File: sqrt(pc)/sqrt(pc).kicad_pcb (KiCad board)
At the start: 2 copper layers, 64 x 39.5 mm, 14 parts, among them U1 WEMOS_C3_mini

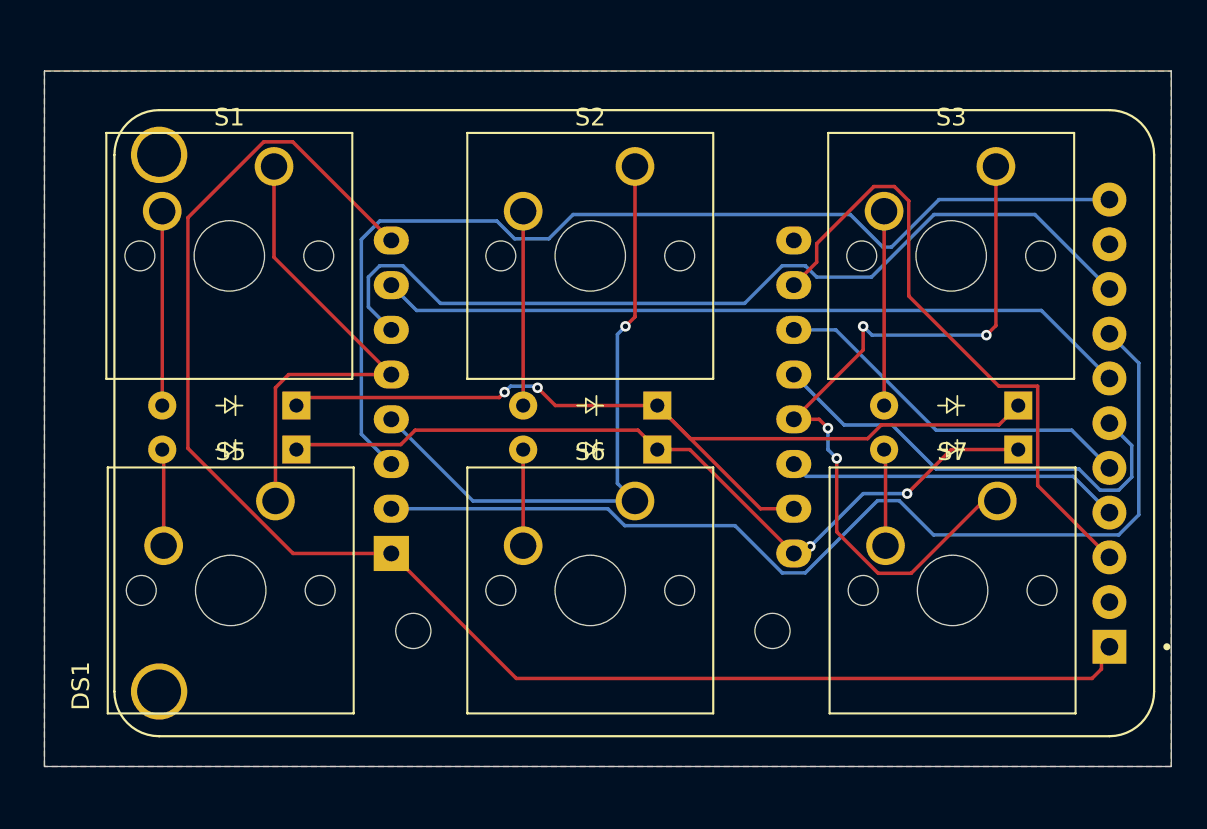
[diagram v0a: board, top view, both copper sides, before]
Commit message: finished wiring PCB
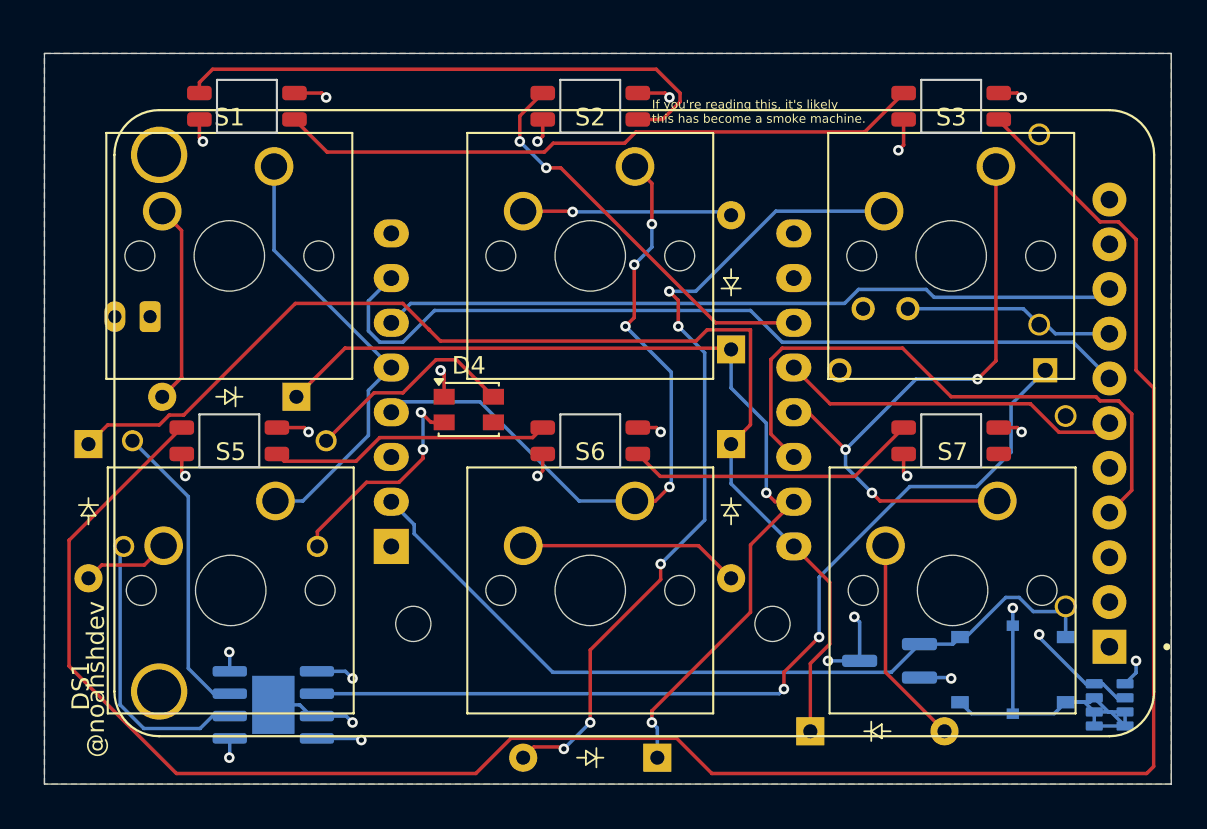
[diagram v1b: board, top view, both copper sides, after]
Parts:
- added C46: 100nF, C315C104K5R5TA:CAPRR254W54L381T254H466B, B.Cu at (79.3, 31.5)
- added D10: LED_SK6812MINI, ScottoKeebs_Components:LED_SK6812MINI, F.Cu at (62.5, 20.0)
- added D11: LED_SK6812MINI, ScottoKeebs_Components:LED_SK6812MINI, F.Cu at (83.0, 20.0)
- added D12: LED_SK6812MINI, ScottoKeebs_Components:LED_SK6812MINI, F.Cu at (42.0, 39.0)
- added D13: LED_SK6812MINI, ScottoKeebs_Components:LED_SK6812MINI, F.Cu at (62.5, 39.0)
- added D14: LED_SK6812MINI, ScottoKeebs_Components:LED_SK6812MINI, F.Cu at (83.0, 39.0)
- added D4: LED_ARBG, LED_SMD:LED_Kingbright_AAA3528ESGCT, F.Cu at (55.6, 37.2)
- added D9: LED_SK6812MINI, ScottoKeebs_Components:LED_SK6812MINI, F.Cu at (43.0, 20.0)
- added J1: Conn_01x02, Connector_JST:JST_PH_B2B-PH-K_1x02_P2.00mm_Vertical, B.Cu at (37.5, 31.9)
- added Q1: AO3401A, Package_TO_SOT_SMD:SOT-23W_Handsoldering, B.Cu at (79.5, 51.5)
- added R2: FMP100JR-52-2K2, KiCADv6:FMP100JR_52_2K2, B.Cu at (88.3, 35.0)
- added R3: MFR-25FBF52-1K, MFR-25FBF52-1K:RESAD1100W55L680D260, B.Cu at (41.5, 45.0)
- added R4: MFR-25FBF52-1K, MFR-25FBF52-1K:RESAD1100W55L680D260, B.Cu at (42.0, 39.0)
- added R5: RNC55H1002FMRE7, RNC55H1002FMRE7:RESAD1081W64L635D269, B.Cu at (88.0, 27.0)
- added R6: RNC55H1002FMRE7, RNC55H1002FMRE7:RESAD1081W64L635D269, B.Cu at (89.5, 43.0)
- added RN1: CAY16-1003F4LF, CAY16-1003F4LF:RESCAF80P320X160X60-8N, B.Cu at (92.0, 54.0)
- added S8: PTS526_SMG15_SMTR2_LFS, PTS526_SMG15_SMTR2_LFS:SW_PTS526_SMG15_SMTR2_LFS, B.Cu at (86.5, 52.0)
- added U2: TP4056-42-ESOP8, Package_SO:SOIC-8-1EP_3.9x4.9mm_P1.27mm_EP2.41x3.3mm, B.Cu at (44.5, 54.0)
- U1: value WEMOS_C3_mini -> WEMOSC3mini
- moved D3 28.6 mm to (66.3, 57.0)
- moved D7 19.9 mm to (75.0, 55.5), turned to 0 degrees
- moved D5 11.8 mm to (34.0, 39.2), turned to -90 degrees
- moved D2 5.27 mm to (70.5, 33.8), turned to 90 degrees
- moved D6 4.20 mm to (70.5, 39.2), turned to -90 degrees
- moved D1 0.50 mm to (45.8, 36.5)
- moved U1 0.40 mm to (51.2, 45.0)
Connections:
- DS1 pad 11: BACKLIGHT -> 3V3
- DS1 pad 5: SPI_DI -> unconnected-(DS1-MISO-Pad5)
- DS1 pad 8: RESET -> Net-(DS1-~{RST})
- U1 pad 11: SPI_DI -> LED_DIN
- U1 pad 2: RESET -> Q1_GATE_HLD
- U1 pad 3: BACKLIGHT -> BAT_ADC
- U1 pad 9: unconnected-(U1-VBus-Pad9) -> 5V-VBus
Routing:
- net BAT+: track 0.00 -> 171.5 mm, vias 0 -> 3
- net GND: track 36.1 -> 197.8 mm, vias 0 -> 9
- net Net-(D11-DOUT): track 0.00 -> 123.2 mm
- net 3V3: track 87.7 -> 186.3 mm, vias 0 -> 8
- net 5V-VBus: track 0.00 -> 86.9 mm, vias 0 -> 3
- net BACKLIGHT: track 59.3 -> 0.00 mm
- net RESET: track 57.9 -> 0.00 mm
- net Net-(U2-PROG): track 0.00 -> 53.1 mm, vias 0 -> 2
- net BAT_ADC: track 0.00 -> 51.3 mm, vias 0 -> 1
- net Q1_GATE_HLD: track 0.00 -> 46.6 mm
- net Net-(D11-DIN): track 0.00 -> 36.8 mm
- net Net-(D3-A): track 11.0 -> 46.8 mm, vias 0 -> 5
- net Net-(D10-DOUT): track 0.00 -> 32.1 mm
- net LED_DIN: track 0.00 -> 23.1 mm, vias 0 -> 2
- net Row 1: track 46.8 -> 68.1 mm, vias 2 -> 0
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- added copper zone on In1.Cu, net (none)
- added copper zone on In2.Cu, net (none)
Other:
- board size 64 x 39.5 mm -> 64 x 41.5 mm
- copper layers 2 -> 4
- board text added: "@noahshdev"
- board text added: "If you're reading this, it's likely this has become a smoke machine."
- board text added: "Please tell me you're not looking for a speaker..."

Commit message: BOM + a lot more I guess
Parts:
- D10, D11, D12, D13, D14, D9: moved to B.Cu
- J1: footprint Connector_JST:JST_PH_B2B-PH-K_1x02_P2.00mm_Vertical -> Connector_Molex:Molex_PicoBlade_53048-0210_1x02_P1.25mm_Horizontal
- R5: moved to F.Cu
- moved R2 58.7 mm to (33.5, 55.8), turned to 90 degrees
- moved R5 45.1 mm to (43.5, 19.5), turned to 180 degrees
- moved D4 28.3 mm to (33.5, 19.5)
- moved R6 14.6 mm to (87.5, 57.5), turned to 180 degrees
- moved R3 13.5 mm to (55.0, 44.5), turned to -90 degrees
- moved RN1 12.6 mm to (79.5, 55.4)
- moved C46 11.9 mm to (68.5, 36.5)
- moved J1 7.96 mm to (33.1, 25.3)
- moved D7 7.46 mm to (67.7, 57.0)
- moved D5 7.02 mm to (33.5, 32.2)
- moved D3 2.50 mm to (63.8, 57.0)
- moved D9 0.50 mm to (43.5, 20.0), turned to 180 degrees
- moved DS1 0.42 mm to (65.0, 37.6)
- moved S5 0.16 mm to (44.5, 42.4)
- moved S1 0.08 mm to (44.5, 23.4)
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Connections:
- D10 pad 4: LED_DIN -> Net-(D10-DIN)
- D11 pad 4: Net-(D11-DIN) -> Net-(D10-DOUT)
- D9 pad 2: Net-(D11-DIN) -> Net-(D10-DIN)
- D9 pad 4: Net-(D10-DOUT) -> LED_DIN
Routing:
- net BAT+: track 171.5 -> 106.9 mm, vias 3 -> 4
- net Net-(DS1-~{RST}): track 12.0 -> 70.5 mm
- net Net-(D11-DIN): track 36.8 -> 0.00 mm
- net Net-(D10-DIN): track 0.00 -> 34.3 mm
- net Net-(D4-GK): track 12.8 -> 44.5 mm, vias 2 -> 1
- net Net-(U2-PROG): track 53.1 -> 23.8 mm, vias 2 -> 0
- net 3V3: track 186.3 -> 215.5 mm
- net 5V-VBus: track 86.9 -> 58.6 mm
- net Net-(D12-DOUT): track 16.1 -> 34.9 mm
- net Net-(D4-RK): track 12.3 -> 30.9 mm, vias 0 -> 3
- net GND: track 197.8 -> 216.1 mm, vias 9 -> 6
- net Col 2: track 35.9 -> 53.4 mm, vias 3 -> 2
- net CS: track 48.2 -> 65.3 mm, vias 0 -> 2
- net BAT_ADC: track 51.3 -> 36.2 mm, vias 1 -> 5
- net Net-(D11-DOUT): track 123.2 -> 108.8 mm, vias 0 -> 2
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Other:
- board size 64 x 41.5 mm -> 63 x 41.5 mm
